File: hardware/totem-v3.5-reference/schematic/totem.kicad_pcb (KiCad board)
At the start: 4 copper layers, 45.8 x 46.4 mm, 136 parts, among them J1 USB4135-GF-A, J2 LiPo 1000mAh, J3 u.FL, Q1 AO3401A, Q2 2N7002, Q3 2N7002, Q4 AO3401A, Q5 2N7002, SW1 power, SW2 SOS, U1 ESP32-WROOM-32E, U2 MAX-M10S, U3 TP4056-42-ESOP8, U4 AP2112K-3.3, U5 ICM-20948

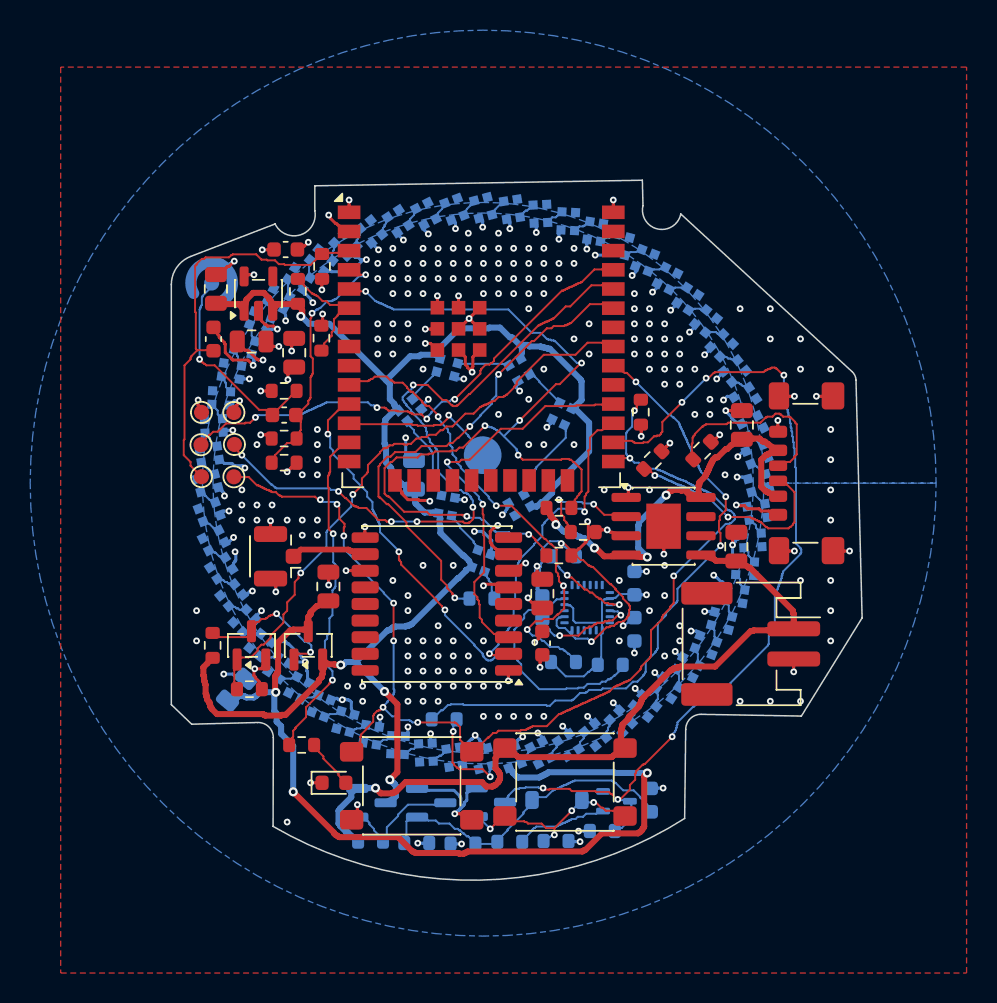
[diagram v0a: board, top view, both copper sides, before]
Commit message: hardware: ST motion sensors, the LED side's missing parts, and a BOM of parts that exist (#12)
Close-up photographs of the reference board's LED side, and a
part-by-part check of the BOM against DigiKey and LCSC, changed the
board.

## LED side: what the close-ups showed

| Reference board | Before this PR | Now |
| --- | --- | --- |
| **Two 0603 LEDs** in the crystal below the touch post, each with an
0603 resistor | Missing; the TP4056's `CHRG`/`STDBY` were left open | D4
(red, charging) and D5 (green, charged) with 1k each, at the
photographed positions. Colours aren't visible unlit; red/green is the
TP4056 convention |
| **Through-hole JST**: its pins' joints show on the LED side, 1.96 mm
apart | SMD JST, 2 mm further in | **S2B-PH-K-S** on the measured pins,
overhanging the corner like the original |
| **Gold SMT pogo pin** as the touch post | Called a "conical spring" |
Same pad; BOM and assembly notes corrected |
| **THT-shell USB-C**: four plated slots at ±4.80 mm, rows 3.0 mm apart,
two holes 6.5 mm apart | USB4135 (SMD) | Unchanged: no catalogue
footprint checked matches that pattern (HRO, GCT USB4105/USB4125, SHOU
HAN 6P and recessed 6P). Recorded in the README with the measurements |
| ~25 small parts in the cluster below the crystal, ~8 in a column by
the ring | This design's own circuit does those jobs | Unchanged;
documented as photographed, not copied. Values and nets can't be read |

## Motion sensing: ST LSM6DSV16X + LIS2MDL

The ICM-20948 is obsolete (DigiKey: "no longer manufactured"). The
LSM6DSV16X sits on its site and the LIS2MDL beside it. Both are on I2C0,
wired to ST's application circuits (DS13510 Fig. 28, DS12144 Fig. 5),
with data-ready lines to IO32/IO33.

From the datasheets, typical values:

| | ICM-20948 | LSM6DSV16X + LIS2MDL |
| --- | --- | --- |
| Gyro noise density | 0.015 dps/√Hz | 0.0028 dps/√Hz |
| Gyro zero-rate drift over temperature | ±0.05 dps/°C | ±0.006 dps/°C |
| Accelerometer noise density | 230 µg/√Hz | 60 µg/√Hz |
| 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
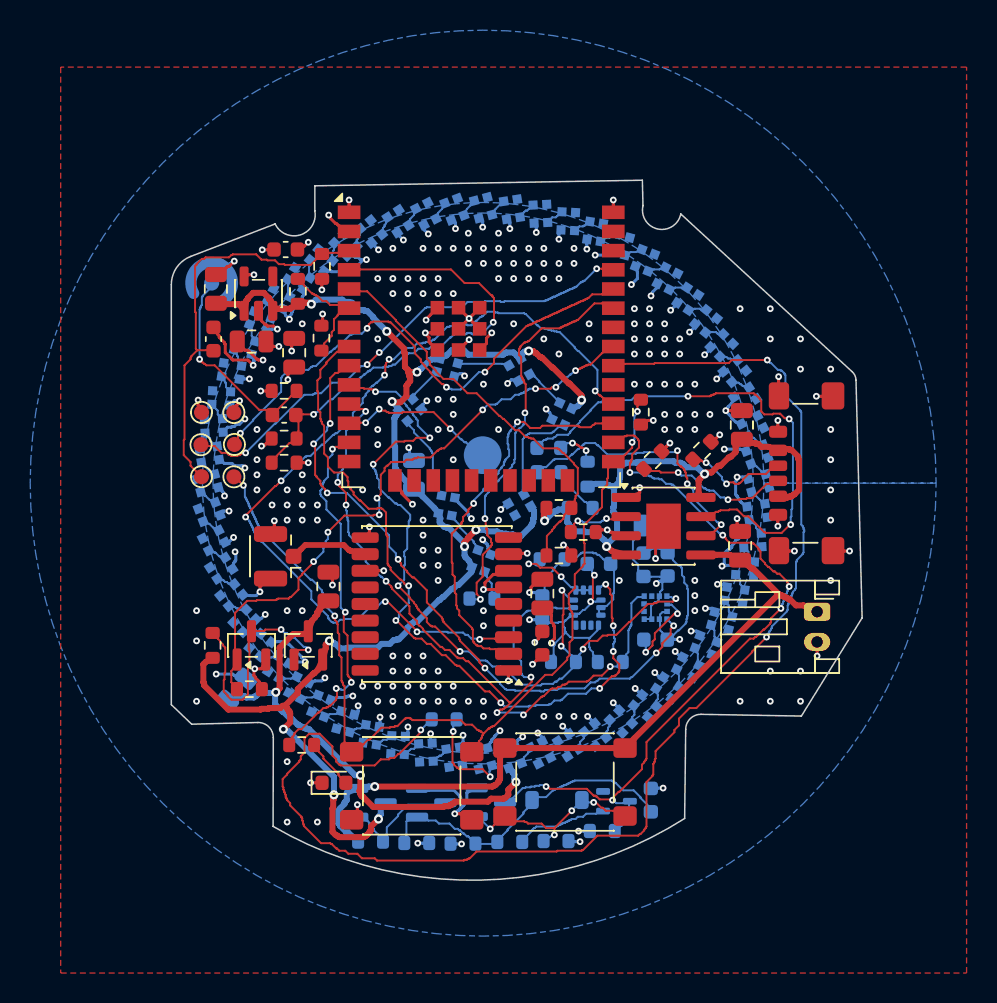
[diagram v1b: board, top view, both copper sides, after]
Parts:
- added C19: 100n, Capacitor_SMD:C_0603_1608Metric, B.Cu at (110.2, 102.9)
- added C20: 10u, Capacitor_SMD:C_0805_2012Metric, B.Cu at (109.4, 100.4)
- added C21: 100n, Capacitor_SMD:C_0603_1608Metric, B.Cu at (108.6, 103.0)
- added D4: red, LED_SMD:LED_0603_1608Metric, B.Cu at (102.3, 95.2)
- added D5: green, LED_SMD:LED_0603_1608Metric, B.Cu at (102.3, 96.8)
- added R27: 1k, Resistor_SMD:R_0603_1608Metric, B.Cu at (104.9, 97.0)
- added R28: 1k, Resistor_SMD:R_0603_1608Metric, B.Cu at (104.4, 99.2)
- added U6: LIS2MDL, Package_LGA:LGA-12_2x2mm_P0.5mm, B.Cu at (109.4, 105.8)
- C8: value 100n -> 220n
- J2: footprint Connector_JST:JST_PH_S2B-PH-SM4-TB_1x02-1MP_P2.00mm_Horizontal -> Connector_JST:JST_PH_S2B-PH-K_1x02_P2.00mm_Horizontal
- R1: value 120k -> 113k
- R2: value 108k -> 102k
- TP1: value touch spring -> touch pogo pin
- U5: value ICM-20948 -> LSM6DSV16X; footprint Sensor_Motion:InvenSense_QFN-24_3x3mm_P0.4mm -> Package_LGA:LGA-14_3x2.5mm_P0.5mm_LayoutBorder3x4y
- moved J2 4.89 mm to (120.1, 106.1)
- moved C7 2.67 mm to (105.6, 102.9), turned to 0 degrees
- moved C8 1.56 mm to (109.4, 107.9), turned to 0 degrees
- moved R26 0.78 mm to (102.5, 102.6)
- moved C11 0.26 mm to (115.0, 101.7)
- moved R8 0.19 mm to (106.4, 109.4)
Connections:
- C1 pad 1: /REGOUT -> +3V3
- C8 pad 1: +3V3 -> /MAG_C1
- R26 pad 1: /IMU_AD0 -> /IMU_SA0
- U1 pad 8: unconnected-(U1-IO32-Pad8) -> /IMU_INT1
- U1 pad 9: unconnected-(U1-IO33-Pad9) -> /MAG_DRDY
- U3 pad 6: unconnected-(U3-~{STDBY}-Pad6) -> /STDBY
- U3 pad 7: unconnected-(U3-~{CHRG}-Pad7) -> /CHRG
- U5 pad 1: unconnected-(U5-NC-Pad1) -> /IMU_SA0
- U5 pad 10: /REGOUT -> unconnected-(U5-OCS_Aux-Pad10)
- U5 pad 12: unconnected-(U5-INT1-Pad12) -> +3V3
- U5 pad 13: +3V3 -> /I2C0_SCL
- U5 pad 14: unconnected-(U5-NC-Pad14) -> /I2C0_SDA
- U5 pad 2: unconnected-(U5-NC-Pad2) -> /IMU_SA0
- U5 pad 3: unconnected-(U5-NC-Pad3) -> /IMU_SA0
- U5 pad 4: unconnected-(U5-NC-Pad4) -> /IMU_INT1
- U5 pad 5: unconnected-(U5-NC-Pad5) -> +3V3
- U5 pad 6: unconnected-(U5-NC-Pad6) -> GND
- U5 pad 7: unconnected-(U5-AUX_CL-Pad7) -> GND
- U5 pad 9: /IMU_AD0 -> unconnected-(U5-INT2-Pad9)
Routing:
- net /RING_DATA: track 41.5 -> 89.8 mm
- net /IMU_INT1: track 0.00 -> 48.2 mm, vias 0 -> 7
- net /MAG_DRDY: track 0.00 -> 42.7 mm, vias 0 -> 7
- net /CHRG: track 0.00 -> 33.6 mm, vias 0 -> 3
- net /GNSS_RX: track 26.8 -> 57.3 mm, vias 2 -> 8
- net /VBUS_SENSE: track 57.2 -> 27.1 mm, vias 7 -> 0
- net VLED: track 58.2 -> 33.7 mm
- net /I2C0_SDA: track 31.8 -> 52.4 mm, vias 4 -> 9
- net /STDBY: track 0.00 -> 18.2 mm, vias 0 -> 3
- net /BTN_SOS: track 74.8 -> 60.1 mm, vias 10 -> 4
- net /MIC: track 17.2 -> 31.7 mm
- net /I2C0_SCL: track 39.4 -> 53.9 mm, vias 3 -> 8
- net /RXD0: track 46.8 -> 34.4 mm, vias 6 -> 4
- net +3V3: track 35.2 -> 46.8 mm, vias 19 -> 20
- net /GPIO4: track 60.1 -> 49.4 mm
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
